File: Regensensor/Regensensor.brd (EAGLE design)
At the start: 114 x 48 mm, 35 parts, among them IC1 LM358N, K1 SMI-2P, T1 BC337, T2 BC327, X1 Output, X2 Heating, X3 Sensor, X4 Supply

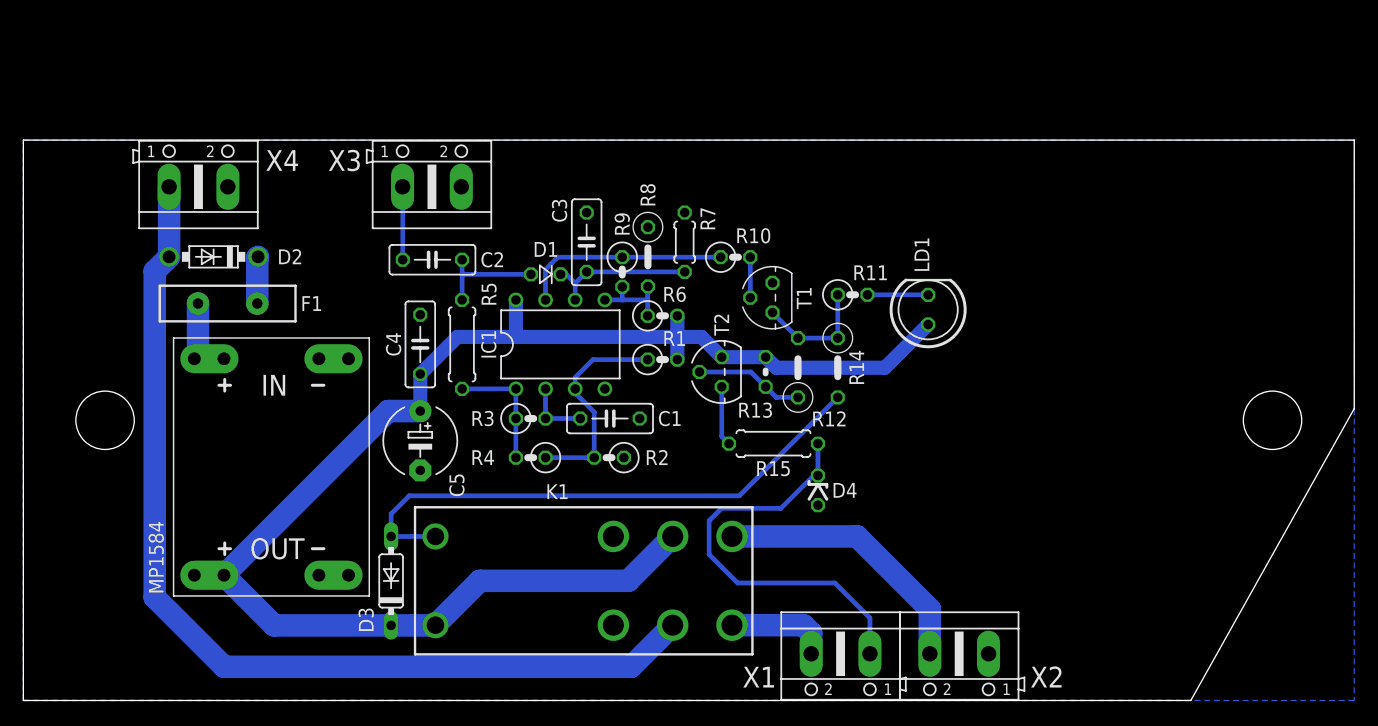
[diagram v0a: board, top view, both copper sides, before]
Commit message: Rework rain sensor board and make it ready for production.
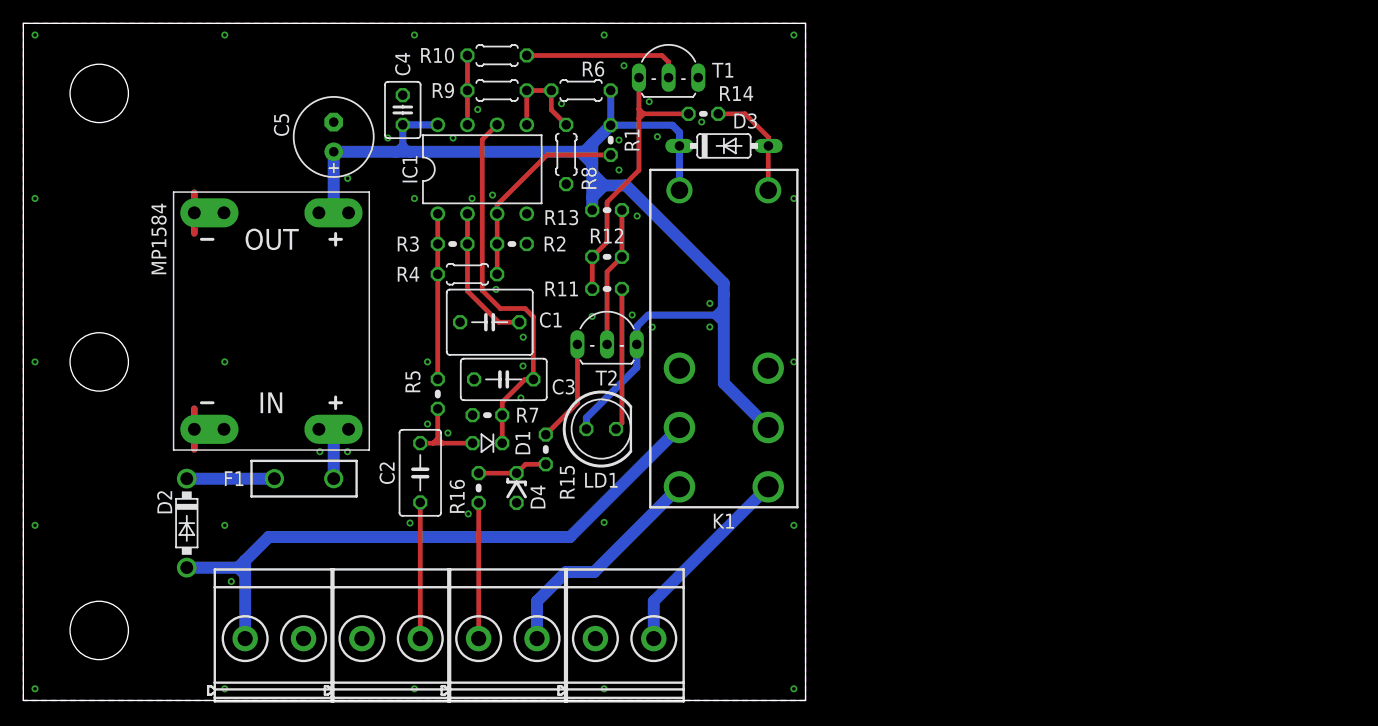
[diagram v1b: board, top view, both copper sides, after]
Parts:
- added R16: 510R, rcl:0204V
- C1: device rcl:C050-025X075 -> rcl:C050-055X075
- C2, C3: device rcl:C050-025X075 -> rcl:C050-035X075
- C4: device rcl:C050-025X075 -> rcl:C025-030X050
- C5: device rcl:E5-6 -> rcl:E2,5-7
- D1: value 1N4148DO35-2V -> 1N4148
- D3: value 1N4148DO35-7 -> 1N4148
- F1: value 3A -> 0.75A; device SparkFun-Fuses:PTH_11MM -> ptc:RGEF250
- K1: device songle:SMI-2P -> songle:SMI
- MP1584: value DC-DC-STEP-DOWN-MP1584 -> 12 V; device modules:DC-DC-STEP-DOWN-MP1584 -> modules:MP1584
- R1, R2, R3: device rcl:0207/2V -> rcl:0204V
- R10, R4, R6, R9: device rcl:0207/2V -> rcl:0204/5
- R11: value 1K -> 510R; device rcl:0207/2V -> rcl:0204V
- R12, R14: device rcl:0207/5V -> rcl:0204V
- R15: value 470R -> 82R; device rcl:0207/7 -> rcl:0204V
- R5: device rcl:0207/7 -> rcl:0204V
- R7: device rcl:0204/5 -> rcl:0204V
- R8: device rcl:0207/5V -> rcl:0204/5
- T1: value BC337 -> BC337-40; device transistor-npn:TO92 -> transistor-small-signal:TO92-LINE
- T2: value BC327 -> BC327-40; device transistor-pnp:TO92 -> transistor-small-signal:TO92-LINE
- X1: value Output -> Supply; device con-ptr500:AK500/2 -> con-phoenix-mkds-3:MKDSB-3/2-2
- X2: value Heating -> Sensor; device con-ptr500:AK500/2 -> con-phoenix-mkds-3:MKDSB-3/2-2
- X3: value Sensor -> Output; device con-ptr500:AK500/2 -> con-phoenix-mkds-3:MKDSB-3/2-2
- X4: value Supply -> Heating; device con-ptr500:AK500/2 -> con-phoenix-mkds-3:MKDSB-3/2-2
- moved X4 53.2 mm to (51.5, 5.30)
- moved X2 48.7 mm to (31.5, 5.30), turned to 0 degrees
- moved X1 48.5 mm to (21.5, 5.30), turned to 0 degrees
- moved D3 46.9 mm to (60.0, 47.5), turned to 0 degrees
- moved X3 39.2 mm to (41.5, 5.30)
- moved LD1 29.8 mm to (49.5, 23.2), turned to 0 degrees
- moved C5 27.1 mm to (26.6, 48.3), turned to 90 degrees
- moved R10 26.8 mm to (40.6, 55.2)
- moved D4 25.8 mm to (42.2, 18.2)
- moved R14 24.6 mm to (58.2, 50.2), turned to 0 degrees
- moved K1 24.0 mm to (60.0, 31.0), turned to 270 degrees
- moved D2 22.9 mm to (14.0, 15.2), turned to 270 degrees
- moved R7 22.5 mm to (39.8, 24.4), turned to 0 degrees
- moved R11 21.0 mm to (50.0, 35.2)
- moved T1 20.8 mm to (55.3, 53.4), turned to 0 degrees
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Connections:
- new net N$20: R16.1, X3.1
- net +24V: now also X1.1; no longer X4.1
- net GND: now also X1.2, X4.1; no longer X3.2, X4.2
- net N$13: now also X2.2; no longer X3.1
- net N$15: now also R16.2; no longer X1.1
- net N$16: now also X3.2; no longer X1.2
- net N$17: now also X4.2; no longer X2.2
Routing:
- net N$14: track 48.1 -> 9.69 mm
- net N$15: track 35.6 -> 6.06 mm
- net +24V: track 84.0 -> 54.7 mm
- net N$3: track 12.8 -> 32.4 mm
- net N$10: track 10.2 -> 24.7 mm
- net GND: track 0.00 -> 14.0 mm, vias 0 -> 51
- net +12V: track 123.5 -> 111.0 mm
- net N$2: track 18.1 -> 5.94 mm
- net N$20: track 0.00 -> 11.6 mm
- net N$16: track 8.84 -> 19.5 mm
- net N$5: track 3.47 -> 13.7 mm
- net N$12: track 5.20 -> 12.2 mm
- net N$6: track 5.52 -> 12.2 mm
- net N$17: track 23.4 -> 17.1 mm
- net N$13: track 6.26 -> 11.7 mm
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- added copper zone on layer 1, net GND
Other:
- board size 114 x 48 mm -> 67 x 58 mm

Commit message: Fix rain sensor capacitor footprint
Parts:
- C5: device rcl:E2,5-7 -> rcl:E5-6
- moved C5 1.27 mm to (26.6, 49.5)
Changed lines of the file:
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@@
 <text x="44" y="12" size="1.27" layer="51" align="bottom-center">+24V</text>
 <text x="39" y="12" size="1.27" layer="51" align="bottom-center">+10V</text>
-<text x="22.5" y="55" size="1.778" layer="51" rot="R180" align="bottom-center">Rain sensor</text>
+<text x="18.5" y="55" size="1.778" layer="51" rot="R180" align="bottom-center">Rain sensor</text>
 <text x="24" y="12" size="1.27" layer="51" align="bottom-center">GND</text>
 <text x="31.5" y="14" size="1.4224" layer="51" align="bottom-center">Sensor</text>
@@
 <wire x1="41.8572" y1="26.47" x2="41.8572" y2="24.47" width="0.254" layer="41"/>
 <wire x1="52.7088" y1="42.2534" x2="51.6948" y2="41.2394" width="0.254" layer="42"/>
-<wire x1="25.6569" y1="49.05" x2="25.6569" y2="47.45" width="0.254" layer="41"/>
-<wire x1="25.6569" y1="49.05" x2="25.6569" y2="47.45" width="0.254" layer="42"/>
-<wire x1="27.5107" y1="49.05" x2="27.5107" y2="47.45" width="0.254" layer="41"/>
-<wire x1="27.5107" y1="49.05" x2="27.5107" y2="47.45" width="0.254" layer="42"/>
 <wire x1="39.1" y1="42.823" x2="41.1" y2="42.823" width="0.254" layer="41"/>
 <wire x1="39.52" y1="43.31" x2="40.21" y2="42.62" width="0.254" layer="41"/>
@@
 <attribute name="VALUE" x="52.1336" y="44.3114" size="1.27" layer="27" ratio="10" rot="R180"/>
 </element>
-<element name="C5" library="rcl" package="E2,5-7" value="47uF" x="26.584" y="48.27" smashed="yes" rot="R90">
-<attribute name="NAME" x="22.75" y="48.27" size="1.27" layer="25" ratio="10" rot="R90"/>
-<attribute name="VALUE" x="29.505" y="51.318" size="1.27" layer="27" ratio="10" rot="R90"/>
+<element name="C5" library="rcl" package="E5-6" value="47uF" x="26.584" y="49.54" smashed="yes" rot="R90">
+<attribute name="NAME" x="22.75" y="49.54" size="1.27" layer="25" ratio="10" rot="R90"/>
+<attribute name="VALUE" x="29.505" y="52.588" size="1.27" layer="27" ratio="10" rot="R90"/>
 </element>
 <element name="X2" library="con-phoenix-mkds-3" package="MKDSB-3/2-2" value="Sensor" x="31.5" y="5.3" smashed="yes">
